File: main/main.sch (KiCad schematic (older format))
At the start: 1 part

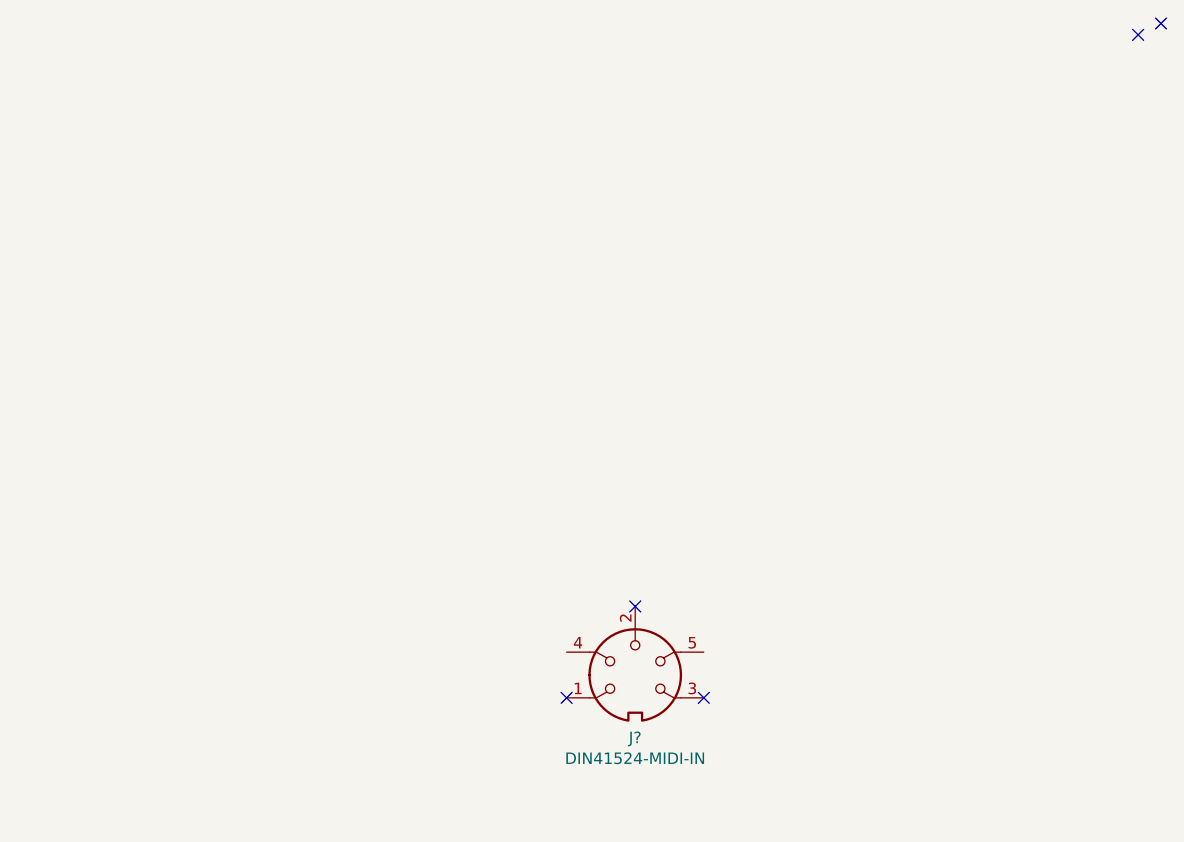
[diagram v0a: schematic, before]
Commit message: Implement MIDI input circuit.
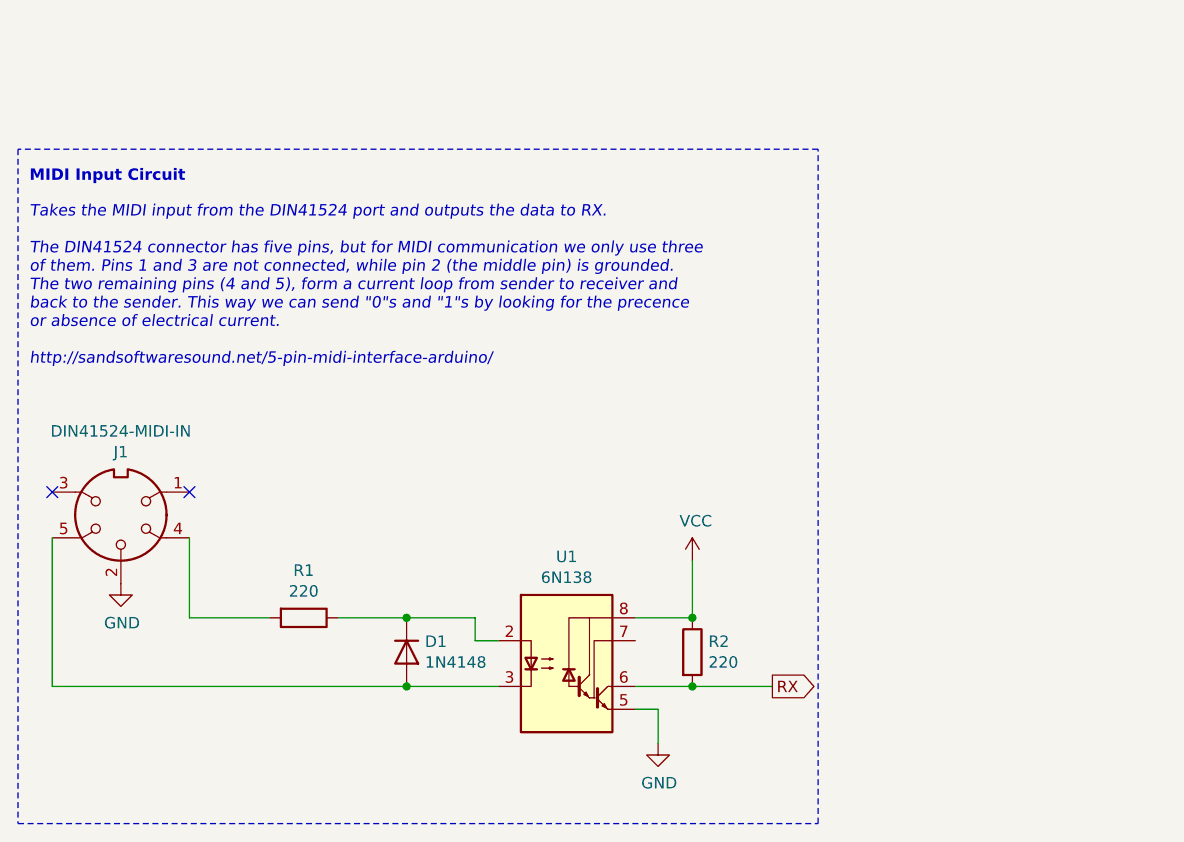
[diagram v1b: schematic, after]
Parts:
- added D1: 1N4148, Diode_THT:D_DO-35_SOD27_P7.62mm_Horizontal, symbol Diode:1N4148
- added R1, R2: 220, symbol Device:R
- added U1: 6N138, symbol Isolator:6N138
- gave numbers to parts that had none: 1
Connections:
- net GND: now reaches J1.2
- net GND: now also U1.5 (GND)
- net at J1.4: now also R1.2
- net at J1.5: now also D1.2 (A), U1.3 (C2)
- new net: D1.1 (K), R1.1, U1.2 (C1)
- new net RX: R2.2, U1.6 (VO2)
- new net VCC: R2.1, U1.8 (VCC)
- no-connect marks 5 -> 2
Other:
- note added: "MIDI Input Circuit"
- note added: "Takes the MIDI input from the DIN41524 port and outputs the data to RX.\n\nThe DIN41524 connector has five pins, but for MIDI communication we only use three\nof them. Pins 1 and 3 are not connected, while pin 2 (the middle pin) is grounded.\nThe two remaining pins (4 and 5), form a current loop from sender to receiver and\nback to the sender. This way we can send "0"s and "1"s by looking for the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"
- moved on the sheet: J1
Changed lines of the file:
@@
 encoding utf-8
 Sheet 1 1
-Title ""
-Date ""
-Rev ""
+Title "Synthesizer"
+Date "2021-09-06"
+Rev "v01"
 Comp ""
 Comment1 ""
 Comment2 ""
 Comment3 ""
-Comment4 ""
+Comment4 "TDT4295 Computer Design Project"
 $EndDescr
-NoConn ~ 5450 4200
-NoConn ~ 5550 4150
 $Comp
-L MIDI:DIN41524-MIDI-IN J?
+L MIDI:DIN41524-MIDI-IN J1
 U 1 1 613702D9
-P 3250 7000
-F 0 "J?" H 3250 6725 50  0000 C CNN
-F 1 "DIN41524-MIDI-IN" H 3250 6634 50  0000 C CNN
-F 2 "" H 3250 7000 50  0001 C CNN
-F 3 "http://www.mouser.com/ds/2/18/40_c091_abd_e-75918.pdf" H 3250 7000 50  0001 C CNN
-	1    3250 7000
+P 1000 6300
+F 0 "J1" H 1000 6025 50  0000 C CNN
+F 1 "DIN41524-MIDI-IN" H 1000 5934 50  0000 C CNN
+F 2 "" H 1000 6300 50  0001 C CNN
+F 3 "http://www.mouser.com/ds/2/18/40_c091_abd_e-75918.pdf" H 1000 6300 50  0001 C CNN
+	1    1000 6300
+	-1   0    0    1
+$EndComp
+NoConn ~ 700  6200
+NoConn ~ 1300 6200
+Wire Notes Line
+	550  4700 550  7650
+Wire Notes Line
+	550  7650 4050 7650
+Wire Notes Line
+	4050 7650 4050 4700
+$Comp
+L power:GND #PWR01
+U 1 1 61363963
+P 1000 6600
+F 0 "#PWR01" H 1000 6350 50  0001 C CNN
+F 1 "GND" H 1005 6427 50  0000 C CNN
+F 2 "" H 1000 6600 50  0001 C CNN
+F 3 "" H 1000 6600 50  0001 C CNN
+	1    1000 6600
 	1    0    0    -1
 $EndComp
-NoConn ~ 3550 7100
-NoConn ~ 2950 7100
-NoConn ~ 3250 6700
+$Comp
+L Diode:1N4148 D1
+U 1 1 61364133
+P 2250 6900
+F 0 "D1" V 2204 6980 50  0000 L CNN
+F 1 "1N4148" V 2295 6980 50  0000 L CNN
+F 2 "Diode_THT:D_DO-35_SOD27_P7.62mm_Horizontal" H 2250 6725 50  0001 C CNN
+F 3 "https://assets.nexperia.com/documents/data-sheet/1N4148_1N4448.pdf" H 2250 6900 50  0001 C CNN
+	1    2250 6900
+	0    1    1    0
+$EndComp
+$Comp
+L Device:R R1
+U 1 1 6136EC29
+P 1800 6750
+F 0 "R1" V 1593 6750 50  0000 C CNN
+F 1 "220" V 1684 6750 50  0000 C CNN
+F 2 "" V 1730 6750 50  0001 C CNN
+F 3 "~" H 1800 6750 50  0001 C CNN
+	1    1800 6750
+	0    1    1    0
+$EndComp
+Wire Wire Line
+	700  6400 700  7050
+Wire Wire Line
+	700  7050 2250 7050
+Wire Wire Line
+	1300 6400 1300 6750
+Wire Wire Line
+	1300 6750 1650 6750
+Wire Wire Line
+	1950 6750 2250 6750
+$Comp
+L Isolator:6N138 U1
+U 1 1 613701F7
+P 2950 6950
+F 0 "U1" H 2950 7417 50  0000 C CNN
+F 1 "6N138" H 2950 7326 50  0000 C CNN
+F 2 "" H 3240 6650 50  0001 C CNN
+F 3 "http://www.onsemi.com/pub/Collateral/HCPL2731-D.pdf" H 3240 6650 50  0001 C CNN
+	1    2950 6950
+	1    0    0    -1
+$EndComp
+Wire Wire Line
+	2250 7050 2650 7050
+Connection ~ 2250 7050
+Wire Wire Line
+	2250 6750 2550 6750
+Wire Wire Line
+	2550 6750 2550 6850
+Wire Wire Line
+	2550 6850 2650 6850
+Connection ~ 2250 6750
+$Comp
+L power:GND #PWR02
+U 1 1 61378C8D
+P 3350 7300
+F 0 "#PWR02" H 3350 7050 50  0001 C CNN
+F 1 "GND" H 3355 7127 50  0000 C CNN
+F 2 "" H 3350 7300 50  0001 C CNN
+F 3 "" H 3350 7300 50  0001 C CNN
+	1    3350 7300
+	1    0    0    -1
+$EndComp
+Wire Wire Line
+	3250 7150 3350 7150
+Wire Wire Line
+	3350 7150 3350 7300
+Wire Wire Line
+	3250 7050 3500 7050
+$Comp
+L Device:R R2
+U 1 1 61379AB2
+P 3500 6900
+F 0 "R2" H 3570 6946 50  0000 L CNN
+F 1 "220" H 3570 6855 50  0000 L CNN
+F 2 "" V 3430 6900 50  0001 C CNN
+F 3 "~" H 3500 6900 50  0001 C CNN
+	1    3500 6900
+	1    0    0    -1
+$EndComp
+Wire Wire Line
+	3250 6750 3500 6750
+$Comp
+L power:VCC #PWR03
+U 1 1 6137A50C
+P 3500 6500
+F 0 "#PWR03" H 3500 6350 50  0001 C CNN
+F 1 "VCC" H 3515 6673 50  0000 C CNN
+F 2 "" H 3500 6500 50  0001 C CNN
+F 3 "" H 3500 6500 50  0001 C CNN
+	1    3500 6500
+	1    0    0    -1
+$EndComp
+Wire Wire Line
+	3500 6750 3500 6500
+Connection ~ 3500 6750
+Text Notes 600  4850 0    50   ~ 10
+MIDI Input Circuit
+Wire Notes Line
+	4050 4700 550  4700
+Text Notes 600  5650 0    50   Italic 0
+Takes the MIDI input from the DIN41524 port and outputs the data to RX.\n\nThe DIN41524 connector has five pins, but for MIDI communication we only use three\nof them. Pins 1 and 3 are not connected, while pin 2 (the middle pin) is grounded.\nThe two remaining pins (4 and 5), form a current loop from sender to receiver and\nback to the sender. This way we can send "0"s and "1"s by looking for the precence\nor absence of electrical current.\n\nhttp://sandsoftwaresound.net/5-pin-midi-interface-arduino/
+Wire Wire Line
+	3500 7050 3850 7050
+Connection ~ 3500 7050
+Text GLabel 3850 7050 2    50   Output ~ 0
+RX
 $EndSCHEMATC

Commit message: Add debug interface
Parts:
- added J2: AudioJack3, symbol Connector:AudioJack3
- added J?: Conn_02x10_Odd_Even, symbol Connector_Generic:Conn_02x10_Odd_Even
- added U2, U? (x3): EFM32GG990F1024, symbol energymicro-efm32:EFM32GG990F1024
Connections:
- net GND: now also J2.S, J?.10 (Pin_10), J?.12 (Pin_12), J?.14 (Pin_14), J?.16 (Pin_16), J?.18 (Pin_18), J?.20 (Pin_20), J?.4 (Pin_4), J?.6 (Pin_6), J?.8 (Pin_8)
- net RX renamed MIDI_RX
- net MIDI_RX: now also U2.E3 (PA4/EBI_AD13_#0-1-2/ETM_TD2_#3/LCD_SEG17/LES_ALTEX3/TIM0_CDTI1_#0/U0_RX_#2)
- new net DAC0: J2.T, U2.L5 (PB11/DAC0_OUT0/OPAMP_OUT0/I2C1_SDA_#1/LETIM0_OUT0_#1/TIM1_CC2_#3)
- new net DAC1: J2.R, U2.L6 (PB12/DAC0_OUT1/OPAMP_OUT1/I2C1_SCL_#1/LETIM0_OUT1_#1)
- new net DBG_SWCLK: J?.9 (Pin_9), U?.E8 (PF0/DBG_SWCLK_#0-1-2-3/I2C0_SDA_#5/LETIM0_OUT0_#2/LEU0_TX_#3/TIM0_CC0_#5/US1_CLK_#2)
- new net DBG_SWDIO: J?.7 (Pin_7), U?.D8 (PF1/DBG_SWDIO_#0-1-2-3/GPIO_EM4WU3/I2C0_SCL_#5/LETIM0_OUT1_#2/LEU0_RX_#3/TIM0_CC1_#5/US1_CS_#2)
- new net DBG_SWO: J?.13 (Pin_13)
- new net RESETn: J?.15 (Pin_15), U?.K6 (~RESET~)
- new net VMCU: J?.1 (Pin_1)
- no-connect marks 2 -> 9
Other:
- note added: "Analog output circuit"
- note added: "EFM32 Debug Interface Circuit"
- note added: "Takes the MIDI input from the DIN41524 port and outputs to the UART_RX on the EFM32GG.\n\nThe DIN41524 connector has five pins, but for MIDI communication we only use three\nof them. Pins 1 and 3 are not connected, while pin 2 (the middle pin) is grounded.\nThe two remaining pins (4 and 5), form a current loop from sender to receiver and\nback to the sender. This way we can send "0"s and "1"s by 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"
- note added: "The debug interface uses the SW-DP protocol. This is a packet based protocol\nthat uses a unidirectional clock signal (DBG_SWCLK) and a bi-directional data\nsignal (DBG_SWDIO). The debugger (usually) drives the clock signal, while\nthe data-line can be driven be either two. The DBG_SWO line is optionally\nincluded for debug output.\n\nhttps://www.silabs.com/documents/public/application-notes/AN00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"
- note removed: "Takes the MIDI input from the DIN41524 port and outputs the data to RX.\n\nThe DIN41524 connector has five pins, but for MIDI communication we only use three\nof them. Pins 1 and 3 are not connected, while pin 2 (the middle pin) is grounded.\nThe two remaining pins (4 and 5), form a current loop from sender to receiver and\nback to the sender. This way we can send "0"s and "1"s by looking for the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"
- moved on the sheet: D1, J1, R1, R2, U1

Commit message: Moved some stuff around
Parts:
- gave numbers to parts that had none: 2
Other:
- note added: "Analog Output"
- note added: "EFM32 Debug Interface"
- note added: "MIDI Input"
- note removed: "Analog output circuit"
- note removed: "EFM32 Debug Interface Circuit"
- note removed: "MIDI Input Circuit"
- moved on the sheet: J2, J3
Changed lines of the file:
@@
 Connection ~ 3500 2600
 Text Notes 600  700  0    50   ~ 10
-MIDI Input Circuit
+MIDI Input
 Text Notes 600  1500 0    50   Italic 0
 Takes the MIDI input from the DIN41524 port and outputs to the UART_RX on the EFM32GG.\n\nThe DIN41524 connector has five pins, but for MIDI communication we only use three\nof them. Pins 1 and 3 are not connected, while pin 2 (the middle pin) is grounded.\nThe two remaining pins (4 and 5), form a current loop from sender to receiver and\nback to the sender. This way we can send "0"s and "1"s by looking for the precence\nor absence of electrical current.\n\nhttp://sandsoftwaresound.net/5-pin-midi-interface-arduino/
@@
 L Connector:AudioJack3 J2
 U 1 1 61366BDF
-P 2850 3900
-F 0 "J2" H 2570 3833 50  0000 R CNN
-F 1 "AudioJack3" H 2570 3924 50  0000 R CNN
-F 2 "" H 2850 3900 50  0001 C CNN
-F 3 "~" H 2850 3900 50  0001 C CNN
-	1    2850 3900
+P 3000 4700
+F 0 "J2" H 2720 4633 50  0000 R CNN
+F 1 "AudioJack3" H 2720 4724 50  0000 R CNN
+F 2 "" H 3000 4700 50  0001 C CNN
+F 3 "~" H 3000 4700 50  0001 C CNN
+	1    3000 4700
 	-1   0    0    1
 $EndComp
@@
 L power:GND #PWR0101
 U 1 1 61367C82
-P 2550 4150
-F 0 "#PWR0101" H 2550 3900 50  0001 C CNN
-F 1 "GND" H 2555 3977 50  0000 C CNN
-F 2 "" H 2550 4150 50  0001 C CNN
-F 3 "" H 2550 4150 50  0001 C CNN
-	1    2550 4150
-	1    0    0    -1
-$EndComp
-Wire Wire Line
-	2550 4150 2550 4000
-Wire Wire Line
-	2550 4000 2650 4000
+P 2700 4950
+F 0 "#PWR0101" H 2700 4700 50  0001 C CNN
+F 1 "GND" H 2705 4777 50  0000 C CNN
+F 2 "" H 2700 4950 50  0001 C CNN
+F 3 "" H 2700 4950 50  0001 C CNN
+	1    2700 4950
+	1    0    0    -1
+$EndComp
+Wire Wire Line
+	2700 4950 2700 4800
+Wire Wire Line
+	2700 4800 2800 4800
 $Comp
 L energymicro-efm32:EFM32GG990F1024 U2
@@
 Text GLabel 11850 6900 0    50   Output ~ 0
 DAC1
-Text GLabel 2650 3800 0    50   Input ~ 0
+Text GLabel 2800 4600 0    50   Input ~ 0
 DAC0
-Text GLabel 2650 3900 0    50   Input ~ 0
+Text GLabel 2800 4700 0    50   Input ~ 0
 DAC1
 Wire Notes Line
 	550  3450 4250 3450
 Wire Notes Line
-	4250 6550 550  6550
+	4250 5250 550  5250
 Text Notes 600  3600 0    50   ~ 10
-Analog output circuit
-Wire Notes Line
-	4250 3450 4250 6550
-Wire Notes Line
-	550  6550 550  3450
+Analog Output
+Wire Notes Line
+	4250 3450 4250 5250
+Wire Notes Line
+	550  5250 550  3450
 NoConn ~ 3250 2700
 Wire Notes Line
@@
 MIDI_RX
 $Comp
-L energymicro-efm32:EFM32GG990F1024 U?
+L energymicro-efm32:EFM32GG990F1024 U3
 U 3 1 61390272
 P 11850 800
-F 0 "U?" H 12150 1050 60  0000 L CNN
+F 0 "U3" H 12150 1050 60  0000 L CNN
 F 1 "EFM32GG990F1024" H 15950 -2100 60  0000 L CNN
 F 2 "" H 11850 800 50  0001 C CNN
@@
 DBG_SWDIO
 Wire Notes Line
-	4300 2900 7500 2900
-Wire Notes Line
-	7500 2900 7500 550
-Wire Notes Line
-	7500 550  4300 550
-Wire Notes Line
-	4300 550  4300 2900
-Text Notes 4350 650  0    50   ~ 10
-EFM32 Debug Interface Circuit
-$Comp
-L Connector_Generic:Conn_02x10_Odd_Even J?
+	550  7650 4250 7650
+Wire Notes Line
+	4250 7650 4250 5300
+Wire Notes Line
+	4250 5300 550  5300
+Wire Notes Line
+	550  5300 550  7650
+Text Notes 600  5400 0    50   ~ 10
+EFM32 Debug Interface
+$Comp
+L Connector_Generic:Conn_02x10_Odd_Even J3
 U 1 1 613A6A76
-P 6700 2050
-F 0 "J?" H 6750 2667 50  0000 C CNN
-F 1 "Conn_02x10_Odd_Even" H 6750 2576 50  0000 C CNN
-F 2 "" H 6700 2050 50  0001 C CNN
-F 3 "~" H 6700 2050 50  0001 C CNN
-	1    6700 2050
-	1    0    0    -1
-$EndComp
-NoConn ~ 7000 1650
-Text GLabel 6500 1950 0    50   BiDi ~ 10
+P 2950 6800
+F 0 "J3" H 3000 7417 50  0000 C CNN
+F 1 "Conn_02x10_Odd_Even" H 3000 7326 50  0000 C CNN
+F 2 "" H 2950 6800 50  0001 C CNN
+F 3 "~" H 2950 6800 50  0001 C CNN
+	1    2950 6800
+	1    0    0    -1
+$EndComp
+NoConn ~ 3250 6400
+Text GLabel 2750 6700 0    50   BiDi ~ 10
 DBG_SWDIO
-Text GLabel 6500 2050 0    50   BiDi ~ 10
+Text GLabel 2750 6800 0    50   BiDi ~ 10
 DBG_SWCLK
-Text GLabel 6500 2250 0    50   Output ~ 10
+Text GLabel 2750 7000 0    50   Output ~ 10
 DBG_SWO
-NoConn ~ 6500 1750
-NoConn ~ 6500 1850
-NoConn ~ 6500 2150
-$Comp
-L energymicro-efm32:EFM32GG990F1024 U?
+NoConn ~ 2750 6500
+NoConn ~ 2750 6600
+NoConn ~ 2750 6900
+$Comp
+L energymicro-efm32:EFM32GG990F1024 U3
 U 2 1 613B0438
 P 17300 850
-F 0 "U?" H 24568 -497 60  0000 L CNN
+F 0 "U3" H 24568 -497 60  0000 L CNN
 F 1 "EFM32GG990F1024" H 24568 -603 60  0000 L CNN
 F 2 "" H 17300 850 50  0001 C CNN
@@
 $EndComp
 $Comp
-L energymicro-efm32:EFM32GG990F1024 U?
+L energymicro-efm32:EFM32GG990F1024 U3
 U 4 1 613B35C7
 P 17300 4200
-F 0 "U?" H 18100 4537 60  0000 C CNN
+F 0 "U3" H 18100 4537 60  0000 C CNN
 F 1 "EFM32GG990F1024" H 18100 4431 60  0000 C CNN
 F 2 "" H 17300 4200 50  0001 C CNN
@@
 Text GLabel 17300 4200 0    50   Input ~ 10
 RESETn
-Text GLabel 6500 2350 0    50   Output ~ 10
+Text GLabel 2750 7100 0    50   Output ~ 10
 RESETn
 $Comp
-L power:GND #PWR?
+L power:GND #PWR04
 U 1 1 613B8CA5
-P 7150 2600
-F 0 "#PWR?" H 7150 2350 50  0001 C CNN
-F 1 "GND" H 7155 2427 50  0000 C CNN
-F 2 "" H 7150 2600 50  0001 C CNN
-F 3 "" H 7150 2600 50  0001 C CNN
-	1    7150 2600
-	1    0    0    -1
-$EndComp
-Wire Wire Line
-	7000 2550 7150 2550
-Wire Wire Line
-	7000 2450 7150 2450
-Wire Wire Line
-	7150 2450 7150 2550
-Connection ~ 7150 2550
-Wire Wire Line
-	7150 2550 7150 2600
-Wire Wire Line
-	7000 2350 7150 2350
-Connection ~ 7150 2450
-Wire Wire Line
-	7000 2250 7150 2250
-Connection ~ 7150 2350
-Wire Wire Line
-	7150 2350 7150 2450
-Wire Wire Line
-	7000 2150 7150 2150
-Wire Wire Line
-	7150 2150 7150 2250
-Connection ~ 7150 2250
-Wire Wire Line
-	7150 2250 7150 2350
-Wire Wire Line
-	7000 2050 7150 2050
-Connection ~ 7150 2150
-Wire Wire Line
-	7000 1950 7150 1950
-Wire Wire Line
-	7150 1950 7150 2050
-Connection ~ 7150 2050
-Wire Wire Line
-	7150 2050 7150 2150
-Wire Wire Line
-	7000 1850 7150 1850
-Connection ~ 7150 1950
-Wire Wire Line
-	7000 1750 7150 1750
-Wire Wire Line
-	7150 1750 7150 1850
-Connection ~ 7150 1850
-Wire Wire Line
-	7150 1850 7150 1950
-NoConn ~ 6500 2450
-NoConn ~ 6500 2550
-Text GLabel 6500 1650 0    50   Output ~ 10
+P 3400 7350
+F 0 "#PWR04" H 3400 7100 50  0001 C CNN
+F 1 "GND" H 3405 7177 50  0000 C CNN
+F 2 "" H 3400 7350 50  0001 C CNN
+F 3 "" H 3400 7350 50  0001 C CNN
+	1    3400 7350
+	1    0    0    -1
+$EndComp
+Wire Wire Line
+	3250 7300 3400 7300
+Wire Wire Line
+	3250 7200 3400 7200
+Wire Wire Line
+	3400 7200 3400 7300
+Connection ~ 3400 7300
+Wire Wire Line
+	3400 7300 3400 7350
+Wire Wire Line
+	3250 7100 3400 7100
+Connection ~ 3400 7200
+Wire Wire Line
+	3250 7000 3400 7000
+Connection ~ 3400 7100
+Wire Wire Line
+	3400 7100 3400 7200
+Wire Wire Line
+	3250 6900 3400 6900
+Wire Wire Line
+	3400 6900 3400 7000
+Connection ~ 3400 7000
+Wire Wire Line
+	3400 7000 3400 7100
+Wire Wire Line
+	3250 6800 3400 6800
+Connection ~ 3400 6900
+Wire Wire Line
+	3250 6700 3400 6700
+Wire Wire Line
+	3400 6700 3400 6800
+Connection ~ 3400 6800
+Wire Wire Line
+	3400 6800 3400 6900
+Wire Wire Line
+	3250 6600 3400 6600
+Connection ~ 3400 6700
+Wire Wire Line
+	3250 6500 3400 6500
+Wire Wire Line
+	3400 6500 3400 6600
+Connection ~ 3400 6600
+Wire Wire Line
+	3400 6600 3400 6700
+NoConn ~ 2750 7200
+NoConn ~ 2750 7300
+Text GLabel 2750 6400 0    50   Output ~ 10
 VMCU
-Text Notes 4350 1250 0    50   Italic 0
+Text Notes 600  6000 0    50   Italic 0
 The debug interface uses the SW-DP protocol. This is a packet based protocol\nthat uses a unidirectional clock signal (DBG_SWCLK) and a bi-directional data\nsignal (DBG_SWDIO). The debugger (usually) drives the clock signal, while\nthe data-line can be driven be either two. The DBG_SWO line is optionally\nincluded for debug output.\n\nhttps://www.silabs.com/documents/public/application-notes/AN0043.pdf
 $EndSCHEMATC
